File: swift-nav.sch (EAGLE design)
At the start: 109 parts, among them J1 SMA_EDGE, J4 PIN_HDR_EDG_1.27MM_5-2, J6 ZX62-B-5PA, U1 6SLX9FTG256, U10 MAX2769, U12 PT7M8206B33TA5EX, U13 M25PX80, U2 LTC3407A, U3 STM32-M-64-LQFP, U4 7Q-16.368MBG-T, U5 SMA_PATCH, U8 B4050, X3 FPGA_DEBUG_HDR

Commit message: Working on the layout
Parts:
- removed C10: 10UF_TANT, jobygnss:10UF_TANT
- added C2: 10uF, rcl:C-USC1206
- C3, C4: value 10UF_TANT -> 10uF; device jobygnss:10UF_TANT -> rcl:C-USC1206
- U13: device jobygnss:M25P80-VMW6TG -> jobygnss:M25P80_MLP8
- U2: value LTC3407A -> LTC3407A_DFN; device jobygnss:LTC3407A -> jobygnss:LTC3407A_DFN
- X1, X2: device pel_molex:CONN_5-1-53261 -> pel_molex:CONN_5-1-53398
- X3: value FPGA_DEBUG_HDR -> (none); device pel_molex:CONN_12-1-53261 -> pel_molex:CONN_8-1-53398
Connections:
- net DEBUG0: now also X3.8; no longer X3.12
- net DEBUG1: now also X3.7; no longer X3.11
- net DEBUG10: no longer X3.2
- net DEBUG2: now also X3.6; no longer X3.10
- net DEBUG3: now also X3.5; no longer X3.9
- net DEBUG4: now also X3.4; no longer X3.8
- net DEBUG5: now also X3.3; no longer X3.7
- net DEBUG6: now also X3.2; no longer X3.6
- net DEBUG7: no longer X3.5
- net DEBUG8: no longer X3.4
- net DEBUG9: no longer X3.3
- net GND: now also C2.2, U13.EP; no longer C10.2
- net V+: now also C2.1; no longer C10.1
- net VCCINT: now also C4.1; no longer C3.1
- net VCCIO: now also C3.1; no longer C4.1

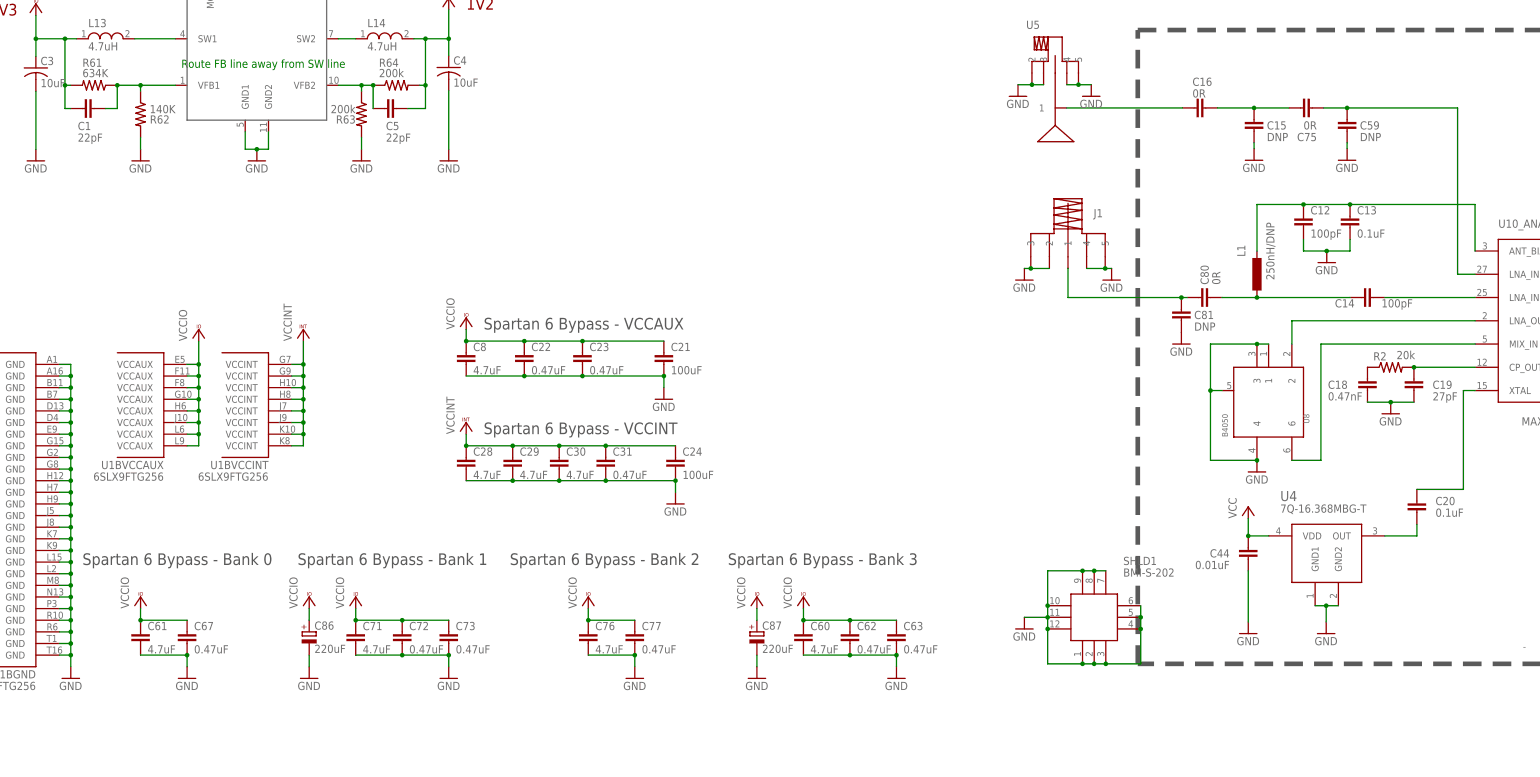
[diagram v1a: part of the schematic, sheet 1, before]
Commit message: Workin on layout. Finished placing everything but a few resistors. Should we size down to a smaller can? Add FTDI 232H?
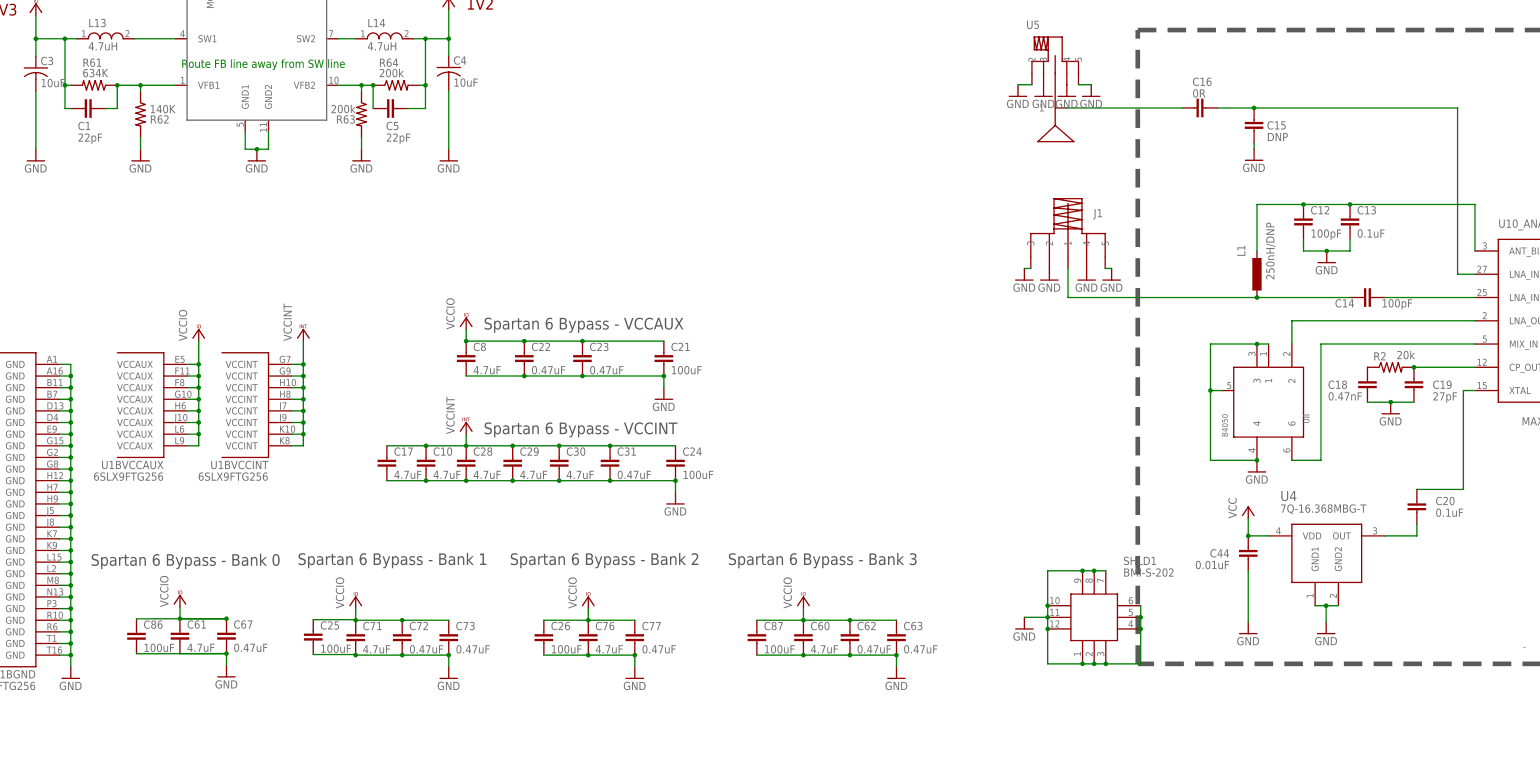
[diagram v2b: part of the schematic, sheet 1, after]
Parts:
- removed C59, C81: DNP, rcl:C-EUC0402
- removed C75, C80: 0R, rcl:C-EUC0402
- removed C83: 100nF, pel_dipol_comp:CAPACITOR-0402
- removed C84: 1uF, pel_dipol_comp:CAPACITOR-POL-1206
- removed C85: 10nF, pel_dipol_comp:CAPACITOR-0402
- added C10, C17: 4.7uF, rcl:C-EUC0603K
- added C25, C26: 100uF, rcl:C-EUC1210K
- added C27: 10nF, rcl:C-EUC0402
- added C32: 100nF, rcl:C-EUC0402
- added C33: 1uF, rcl:C-EUC0603K
- C15, C16: device rcl:C-EUC0402 -> rcl:C-EUC0603K
- C51: device capsmd:C0603 -> rcl:C-EUC0603K
- C86, C87: value 220uF -> 100uF; device pel_dipol_comp:CAPACITOR-POLC -> rcl:C-EUC1210K
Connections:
- removed net 4: U5.4, U5.5
- removed net N$46: C14.1, C80.1, L1.1
- removed net N$9: C15.2, C16.1, C75.1
- net 3: no longer J1.2
- net 5: no longer J1.4
- net GND: now also C10.2, C17.2, C25.2, C26.2, C27.2, C32.2, C33.1, C86.2, C87.2, J1.2, J1.4, U5.4, U5.5; no longer C59.1, C81.1, C83.1, C84.-, C85.1, C86.-, C87.-
- net JTAG_RST: now also C32.1; no longer C83.2
- net N$11: now also C15.2, C16.1; no longer C59.2, C75.2
- net N$8: now also C14.1, L1.1; no longer C80.2, C81.2
- net VCCINT: now also C10.1, C17.1
- net VCCIO: now also C25.1, C26.1, C27.1, C33.2, C86.1, C87.1; no longer C84.+, C85.2, C86.+, C87.+
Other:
- moved on the sheet: C31, C61, C67

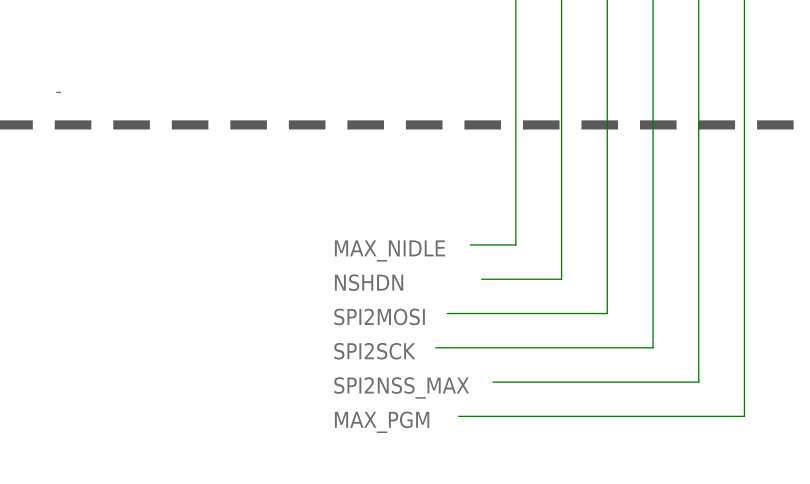
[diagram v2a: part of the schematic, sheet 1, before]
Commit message: RF section routed
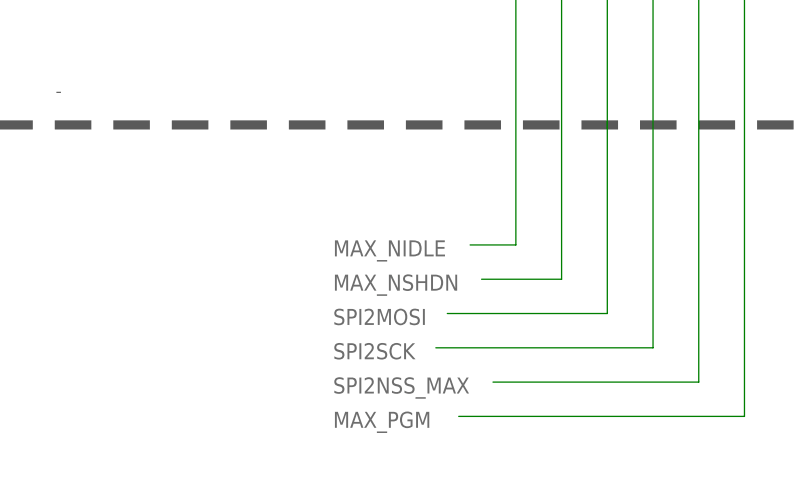
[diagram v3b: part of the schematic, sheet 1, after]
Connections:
- removed net NSHDN: U10_DIG.SHDN
- net MAX_NSHDN: now also U10_DIG.SHDN
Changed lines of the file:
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@@
 <setting verticaltext="up"/>
 </settings>
-<grid distance="1" unitdist="mil" unit="mil" style="lines" multiple="1" display="yes" altdistance="0.01" altunitdist="inch" altunit="inch"/>
+<grid distance="0.1" unitdist="inch" unit="inch" style="lines" multiple="1" display="no" altdistance="0.01" altunitdist="inch" altunit="inch"/>
 <layers>
 <layer number="1" name="Top" color="4" fill="1" visible="no" active="no"/>
@@
 </segment>
 </net>
-<net name="NSHDN" class="0">
+<net name="MAX_NSHDN" class="0">
 <segment>
 <wire x1="462.915" y1="91.44" x2="419.735" y2="91.44" width="0.1524" layer="91"/>

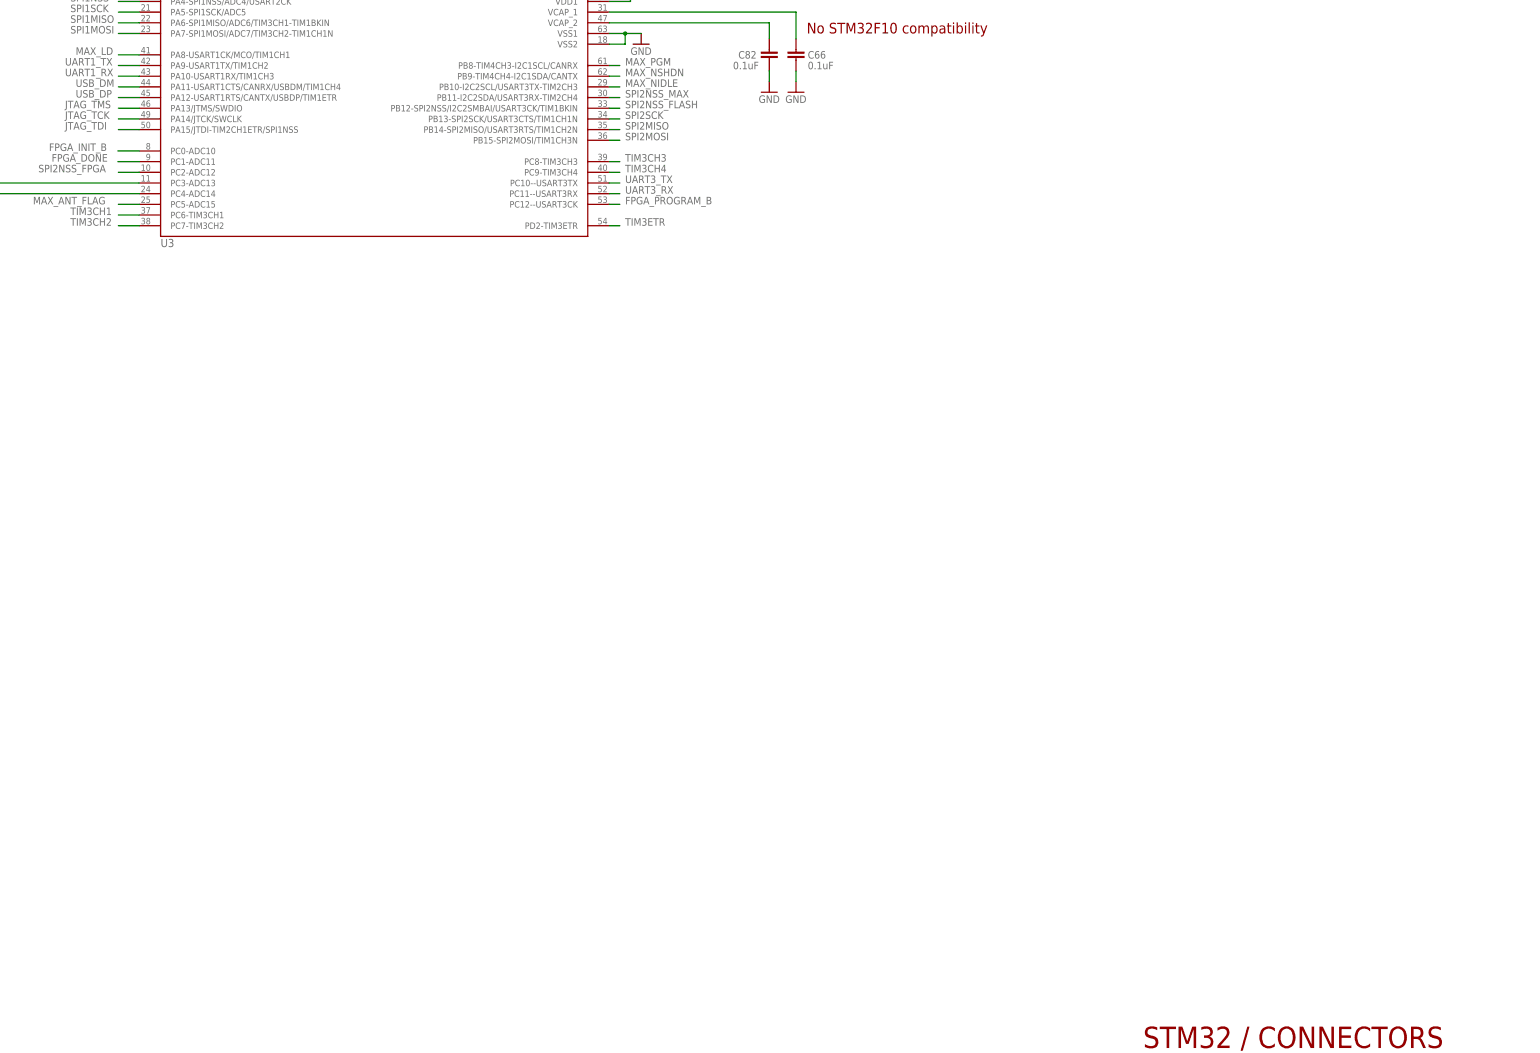
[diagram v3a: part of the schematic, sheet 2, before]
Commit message: Starting placing FT232H components
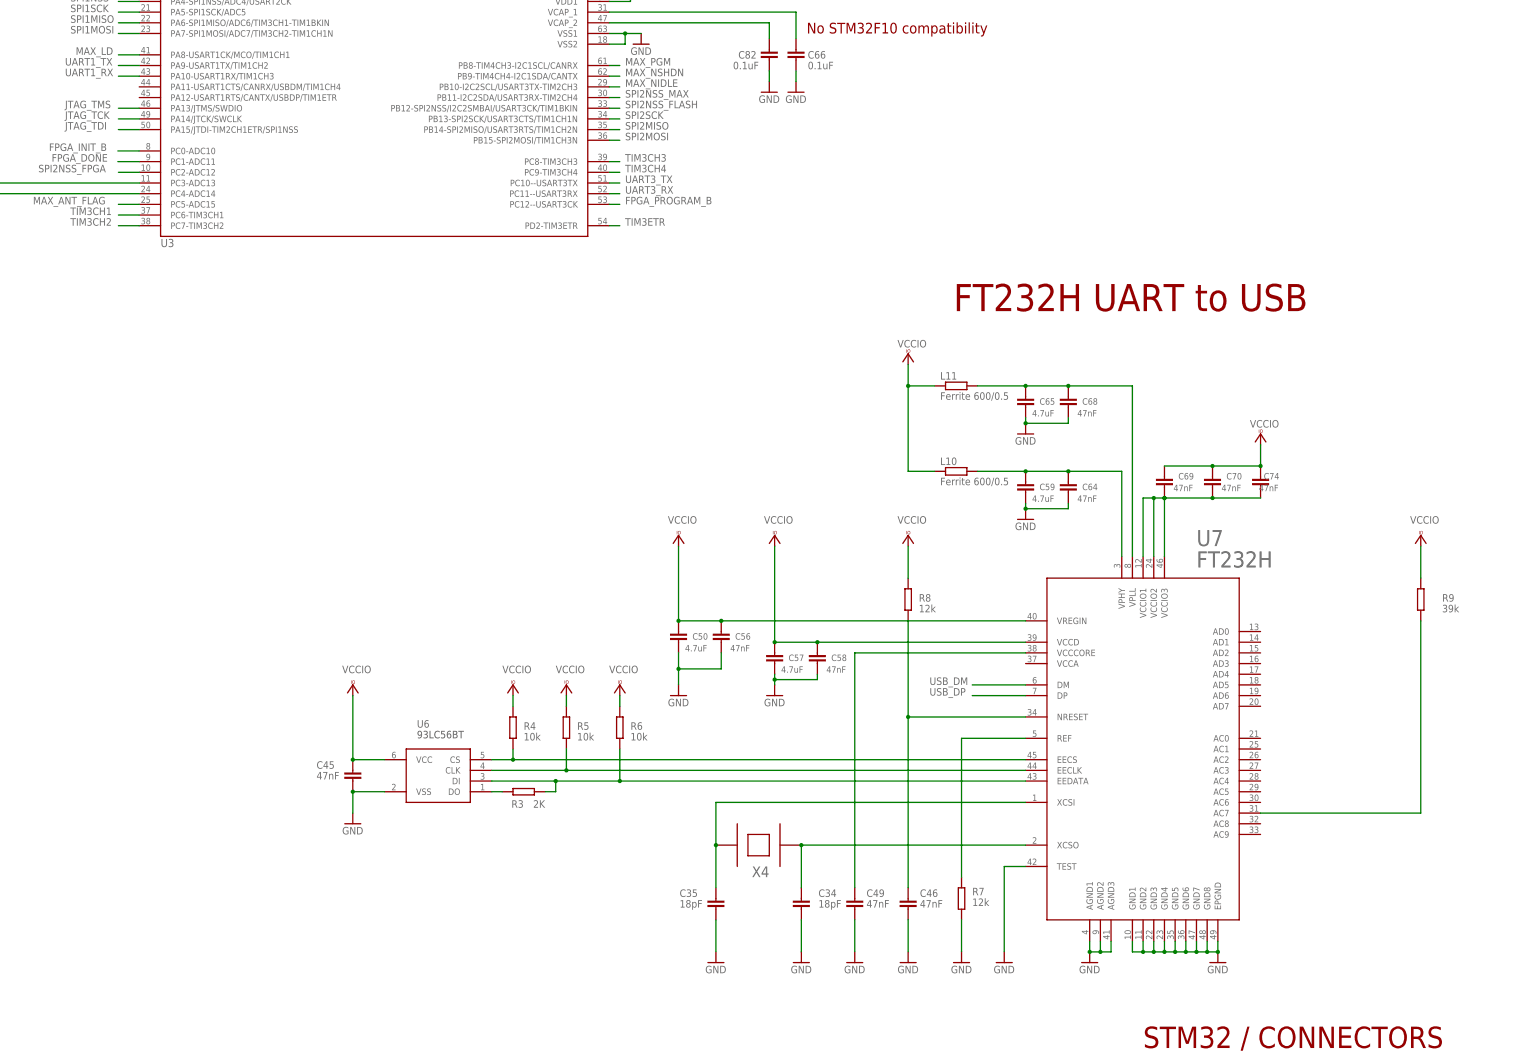
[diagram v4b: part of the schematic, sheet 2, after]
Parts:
- added C34, C35: 18pF, rcl:C-EUC0402
- added C45, C46, C49: 47nF, rcl:C-EUC0402
- added C50, C57, C59, C65: 4.7uF, rcl:C-EUC0603K
- added C56, C58, C64, C68, C69, C70, C74: 47nF, rcl:C-EUC0603K
- added L10, L11: Ferrite 600/0.5, rcl:R-EU_R0805
- added R3: 2K, pel_dipol_comp:RESISTOR-0402
- added R4, R5, R6: 10k, pel_dipol_comp:RESISTOR-0402
- added R7, R8: 12k, pel_dipol_comp:RESISTOR-0402
- added R9: 39k, pel_dipol_comp:RESISTOR-0402
- added U6: 93LC56BT-I/OT, swift-nav:93LC56BT-I/OT
- added U7: FT232HQ, swift-nav:FT232HQ
- added X4: 12MHz, swift-nav:ABLS-12.000MHZ
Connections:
- new net N$15: C35.1, U7.XCSI, X4.1
- new net N$18: C46.1, R8.2, U7.NRESET
- new net N$19: C49.1, U7.VCCCORE
- new net N$20: R9.2, U7.AC7
- new net N$21: C65.2, C68.1, L11.2, U7.VPLL
- new net N$23: R4.2, U6.CS, U7.EECS
- new net N$25: R5.2, U6.CLK, U7.EECLK
- new net N$27: R3.1, R6.2, U6.DI, U7.EEDATA
- new net N$28: R3.2, U6.DO
- new net N$29: C59.2, C64.1, L10.2, U7.VPHY
- new net N$33: R7.1, U7.REF
- new net N$35: C69.2, C70.2, C74.2, U7.VCCIO1, U7.VCCIO2, U7.VCCIO3
- new net N$9: C34.1, U7.XCSO, X4.2
- net GND: now also C34.2, C35.2, C45.2, C46.2, C49.2, C50.1, C56.2, C57.1, C58.2, C59.1, C64.2, C65.1, C68.2, R7.2, U6.VSS, U7.AGND1, U7.AGND2, U7.AGND3, U7.EPGND, U7.GND1, U7.GND2, U7.GND3, U7.GND4, U7.GND5, U7.GND6, U7.GND7, U7.GND8, U7.TEST
- net USB_DM: now also U7.DM; no longer U3.PA11-USART1CTS/CANRX/USBDM/TIM1CH4
- net USB_DP: now also U7.DP; no longer U3.PA12-USART1RTS/CANTX/USBDP/TIM1ETR
- net VCCIO: now also C45.1, C50.2, C56.1, C57.2, C58.1, C69.1, C70.1, C74.1, L10.1, L11.1, R4.1, R5.1, R6.1, R8.1, R9.1, U6.VCC, U7.VCCD, U7.VREGIN
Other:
- note added: "FT232H UART to USB"

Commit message: Hooking up FTDI to FPGA
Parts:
- removed C46: 47nF, rcl:C-EUC0402
- removed R8: 12k, pel_dipol_comp:RESISTOR-0402
- added C75: 47nF, rcl:C-EUC0402
- added D1: MBR0520, swift-nav:MBR0520
- C34, C35: value 18pF -> 20pF
- X4: value 12MHz -> ECS-120-20-3X-TR; device swift-nav:ABLS-12.000MHZ -> swift-nav:ECS-120-20-3X-TR
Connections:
- removed net N$18: C46.1, R8.2, U7.NRESET
- removed net N$35: C69.2, C70.2, C74.2, U7.VCCIO1, U7.VCCIO2, U7.VCCIO3
- new net ADBUS5: U7.AD5
- new net ADBUS6: U7.AD6
- new net ADBUS7: U7.AD7
- new net FTDI_CLKOUT: U7.AC5
- new net FTDI_NOE: U7.AC6
- new net FTDI_NRD: U7.AC2
- new net FTDI_NRST: U3.PB1-ADC9/TIM3CH4-TIM1CH3N, U7.NRESET
- new net FTDI_NRXF: U7.AC0
- new net FTDI_NSIWU: U7.AC4
- new net FTDI_NTXE: U7.AC1
- new net FTDI_NWR: U7.AC3
- new net N$32: C75.1, U7.VCCA
- new net UART6_RX: U3.PC7-TIM3CH2, U7.AD0
- new net UART6_TX: U3.PC6-TIM3CH1, U7.AD1
- new net V_USB: D1.1, J6.1, U3.PB0-ADC8/TIM3CH3-TIM1CH2N
- net GND: now also C69.2, C70.2, C74.2, C75.2; no longer C46.2
- net TIM3CH1: no longer U3.PC6-TIM3CH1
- net TIM3CH2: no longer U3.PC7-TIM3CH2
- net V+: now also D1.2; no longer J6.1
- net VCCIO: now also U7.VCCIO1, U7.VCCIO2, U7.VCCIO3; no longer R8.1
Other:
- moved on the sheet: C34, C35, C45, C49, C50, C56, C57, C58, C59, C64, C65, C68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

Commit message: All components placed, but clearances aren't going to be enough for assembly so have to move stuff to the bottom side.
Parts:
- removed J4: PIN_HDR_EDG_1.27MM_5-2, pel_misc:CONN_5-2-FTSH-V
- added X5: CONN_5-2, pel_misc:CONN_5-2
- X4: value ECS-120-20-3X-TR -> NX5032GA-12M; device swift-nav:ECS-120-20-3X-TR -> swift-nav:NX5032GA-12M
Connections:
- removed net ADBUS5: U7.AD5
- removed net ADBUS6: U7.AD6
- removed net ADBUS7: U7.AD7
- removed net DEBUG10: U1B3.IO_L37N_M3DQ1_3
- removed net DEBUG7: U1B3.IO_L35P_M3DQ10_3
- removed net DEBUG8: U1B3.IO_L36N_M3DQ9_3
- removed net DEBUG9: U1B3.IO_L36P_M3DQ8_3
- removed net FTDI_NOE: U7.AC6
- removed net FTDI_NRD: U7.AC2
- removed net FTDI_NRXF: U7.AC0
- removed net FTDI_NSIWU: U7.AC4
- new net FTDI_ADBUS5: U1B3.IO_L47P_M3A0_3, U7.AD5
- new net FTDI_ADBUS6: U1B3.IO_L48N_M3BA1_3, U7.AD6
- new net FTDI_ADBUS7: U1B3.IO_L48P_M3BA0_3, U7.AD7
- net FTDI_CLKOUT: now also U1B3.IO_L44P_GCLK21_M3A5_3
- net FTDI_NTXE: now also U1B3.IO_L45N_M3ODT_3
- net FTDI_NWR: now also U1B3.IO_L45P_M3A3_3
- net GND: now also X5.3, X5.5, X5.7, X5.9; no longer J4.3, J4.5, J4.7, J4.9
- net JTAG_RST: now also X5.10; no longer J4.10
- net JTAG_TCK: now also X5.4; no longer J4.4
- net JTAG_TDI: now also X5.8; no longer J4.8
- net JTAG_TDO: now also X5.6; no longer J4.6
- net JTAG_TMS: now also X5.2; no longer J4.2
- net VCCIO: now also U7.AC2, U7.AC6, X5.1; no longer J4.1
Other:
- note added: "Change to 10k?"
- moved on the sheet: R9
